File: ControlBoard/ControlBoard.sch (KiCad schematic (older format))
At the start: 76 parts, among them J1 PowerIn, J10 Conn_01x01, J11 Conn_01x01, J2 UART, J3 ICSP, J4 MTR1, J5 MTR2, J8 Conn_01x01, J9 Conn_01x01, Q1 2N3904, SW1 SW_Push, U1 LM358, U5 ATMEGA328P-PU, U6 LM7805_TO220, U7 74HC595, U8 L298D, U9 74HC595, Y1 16MHz

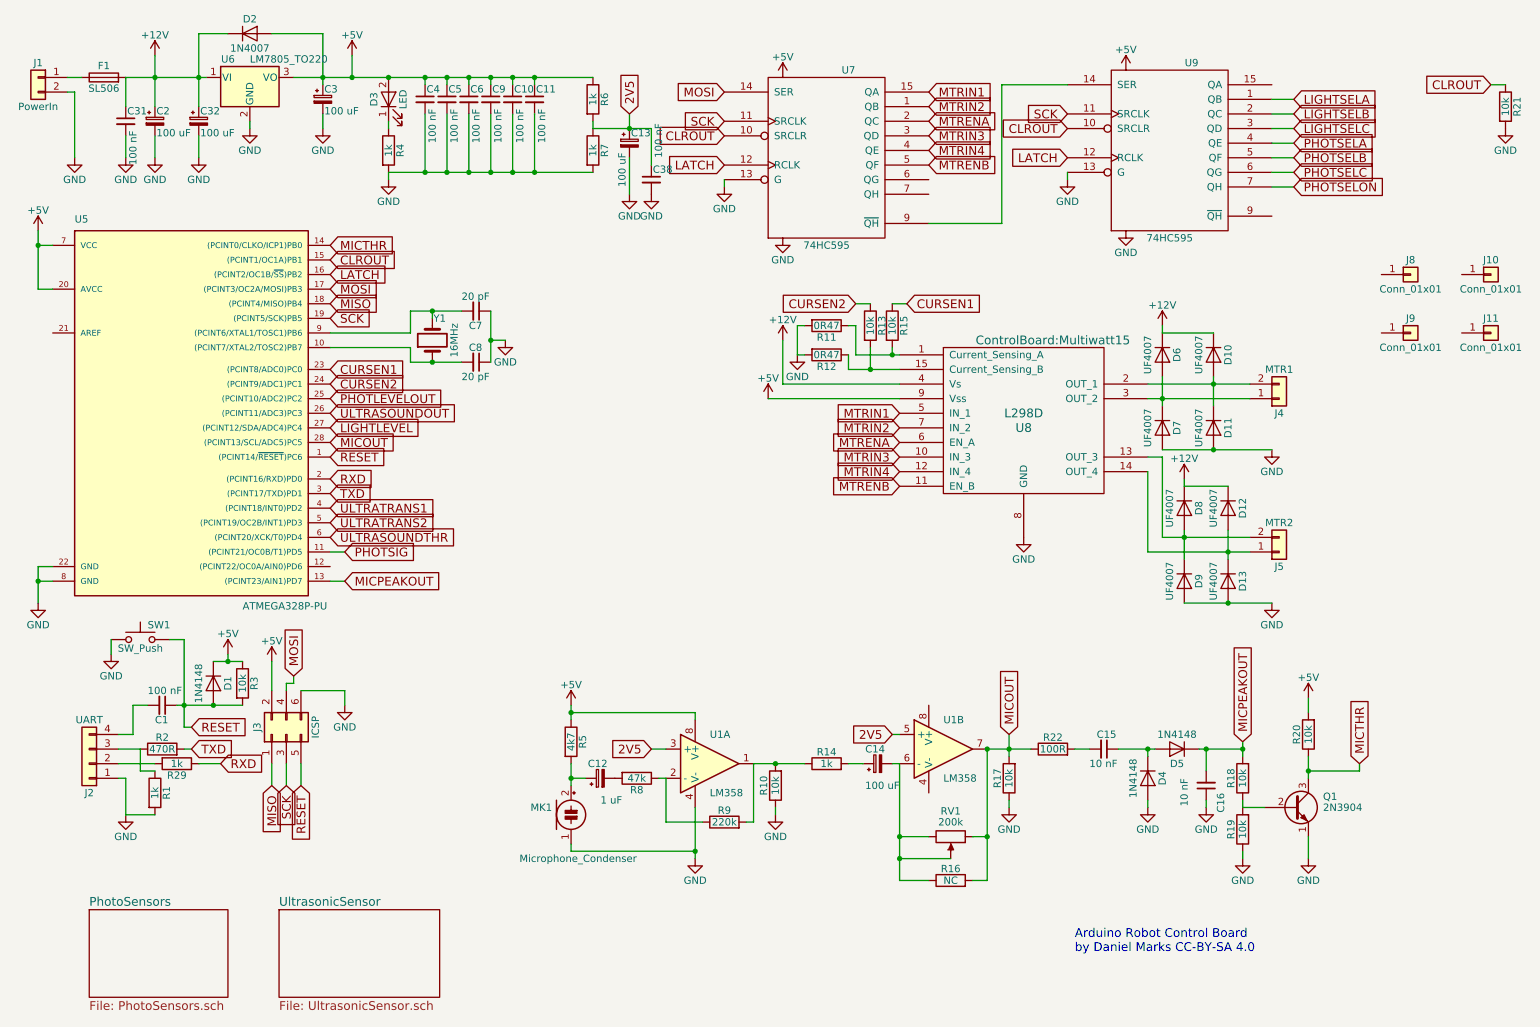
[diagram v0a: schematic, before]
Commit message: Added CAD models
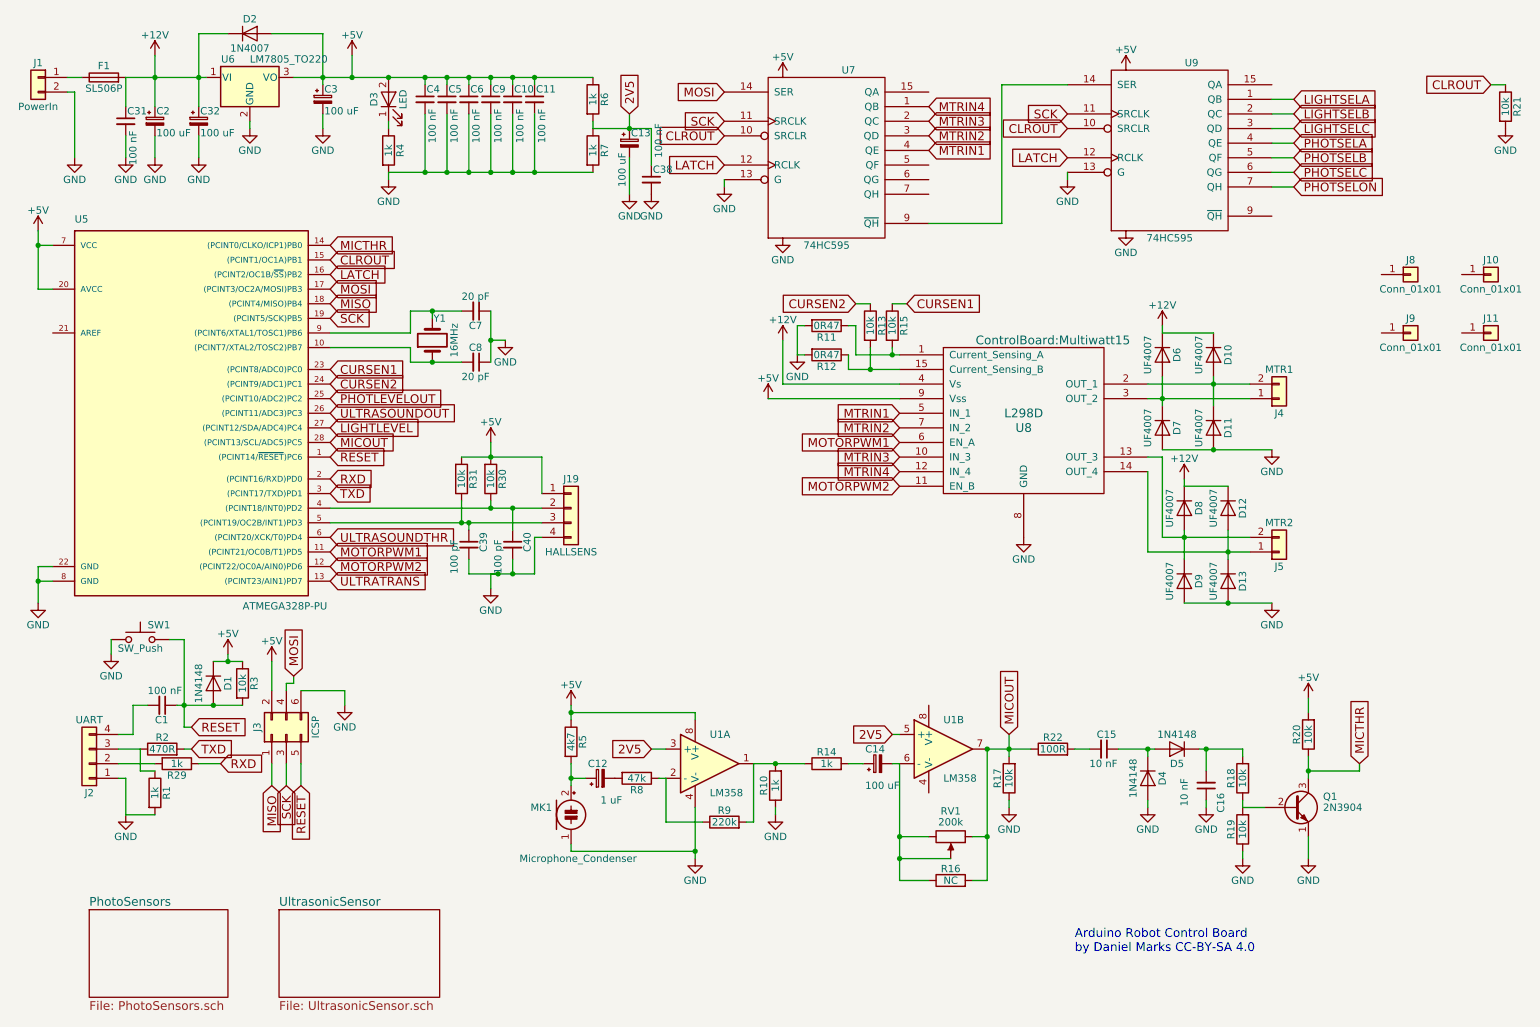
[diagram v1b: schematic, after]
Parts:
- added C39, C40: 100 pF, Capacitors_THT:C_Disc_D5.0mm_W2.5mm_P5.00mm, symbol C_Small
- added J19: HALLSENS, Pin_Headers:Pin_Header_Straight_1x04_Pitch2.54mm, symbol Conn_01x04
- added R30, R31: 10k, Resistors_THT:R_Axial_DIN0207_L6.3mm_D2.5mm_P7.62mm_Horizontal, symbol R
- F1: value SL506 -> SL506P
- R10: value 10k -> 1k
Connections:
- net PHOTSIG is gone; now on net MOTORPWM1: U5.11 ((PCINT21/OC0B/T1)PD5)
- net +5V: now also J19.1 (Pin_1), R30.2, R31.2
- net GND: now also C39.2, C40.2, J19.4 (Pin_4)
- net MTRIN1: now also U7.4 (QE); no longer U7.15 (QA)
- net MTRIN2: now also U7.3 (QD); no longer U7.1 (QB)
- net MTRIN3: now also U7.2 (QC); no longer U7.3 (QD)
- net MTRIN4: now also U7.1 (QB); no longer U7.4 (QE)
- net MOTORPWM2: now reaches U5.12 ((PCINT22/OC0A/AIN0)PD6)
- net MOTORPWM2: now also U8.11 (EN_B)
- net MICPEAKOUT: no longer names the net of C16.2, D5.1 (K), R18.2
- net MICPEAKOUT: no longer U5.13 ((PCINT23/AIN1)PD7)
- net MTRENA renamed MOTORPWM1
- net MOTORPWM1: no longer U7.2 (QC)
- net MTRENB: no longer names the net of U7.5 (QF)
- net MTRENB: no longer U8.11 (EN_B)
- net ULTRATRANS1: no longer names the net of U5.4 ((PCINT18/INT0)PD2)
- net ULTRATRANS1: now also C40.1, J19.2 (Pin_2), R30.1
- net ULTRATRANS2: no longer names the net of U5.5 ((PCINT19/OC2B/INT1)PD3)
- net ULTRATRANS2: now also C39.1, J19.3 (Pin_3), R31.1
- new net ULTRATRANS: U5.13 ((PCINT23/AIN1)PD7)

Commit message: Added KeypadPI
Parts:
- added C44, C45: 100 pF, Capacitors_THT:C_Disc_D5.0mm_W2.5mm_P5.00mm, symbol C_Small
- added C46: 100 nF, Capacitors_THT:C_Disc_D5.0mm_W2.5mm_P2.50mm, symbol C_Small
- added J20: Conn_01x06, Pin_Headers:Pin_Header_Straight_1x06_Pitch2.54mm, symbol Conn_01x06
- added J21: HALLSENS2, Pin_Headers:Pin_Header_Straight_1x04_Pitch2.54mm, symbol Conn_01x04
- added R34, R49, R65: 10k, Resistors_THT:R_Axial_DIN0207_L6.3mm_D2.5mm_P7.62mm_Horizontal, symbol R
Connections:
- net MISO is gone; now on net MICTHR: J3.1 (Pin_1), U5.18 ((PCINT4/MISO)PB4)
- net +5V: now also R21.1, J20.6 (Pin_6), J21.1 (Pin_1), R34.2, R49.2
- net CLROUT: now also R21.2, C46.1; no longer R21.1, U5.15 ((PCINT1/OC1A)PB1)
- net GND: now also C44.2, C45.2, C46.2, J20.1 (Pin_1), J21.4 (Pin_4); no longer R21.2
- net MICTHR: now also R65.2; no longer Q1.3 (C), R20.1, U5.14 ((PCINT0/CLKO/ICP1)PB0)
- net at U7.15 (QA): now also J20.5 (Pin_5)
- net at U7.5 (QF): now also J20.2 (Pin_2)
- net at U7.6 (QG): now also J20.3 (Pin_3)
- net at U7.7 (QH): now also J20.4 (Pin_4)
- new net: C45.1, J21.2 (Pin_2), R49.1, U5.14 ((PCINT0/CLKO/ICP1)PB0)
- new net: C44.1, J21.3 (Pin_3), R34.1, U5.15 ((PCINT1/OC1A)PB1)
- new net: Q1.3 (C), R20.1, R65.1
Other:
- moved on the sheet: C7, C8, R21, Y1

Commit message: JLCPCB order 2021-10-03
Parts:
- added C47: 100 uF, Capacitors_THT:CP_Radial_D5.0mm_P2.50mm, symbol CP_Small
- added J22: PowerIn, Connectors_Terminal_Blocks:TerminalBlock_bornier-2_P5.08mm, symbol Conn_01x02
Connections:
- net +5V: now also C47.1, J22.1 (Pin_1)
- net GND: now also C47.2, J22.2 (Pin_2)
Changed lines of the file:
@@
 $EndComp
 $Comp
-L GND #PWR50
+L GND #PWR53
 U 1 1 6146DC53
 P 10650 1800
-F 0 "#PWR50" H 10650 1550 50  0001 C CNN
+F 0 "#PWR53" H 10650 1550 50  0001 C CNN
 F 1 "GND" H 10650 1650 50  0000 C CNN
 F 2 "" H 10650 1800 50  0001 C CNN
@@
 Connection ~ 10650 1500
 $Comp
-L +5V #PWR49
+L +5V #PWR52
 U 1 1 614E555C
 P 10650 1000
-F 0 "#PWR49" H 10650 850 50  0001 C CNN
+F 0 "#PWR52" H 10650 850 50  0001 C CNN
 F 1 "+5V" H 10650 1140 50  0000 C CNN
 F 2 "" H 10650 1000 50  0001 C CNN
@@
 Wire Wire Line
 	9750 5150 9750 5250
+$Comp
+L Conn_01x02 J22
+U 1 1 6152297D
+P 9800 3250
+F 0 "J22" H 9800 3350 50  0000 C CNN
+F 1 "PowerIn" H 9800 3050 50  0000 C CNN
+F 2 "Connectors_Terminal_Blocks:TerminalBlock_bornier-2_P5.08mm" H 9800 3250 50  0001 C CNN
+F 3 "" H 9800 3250 50  0001 C CNN
+	1    9800 3250
+	-1   0    0    -1
+$EndComp
+$Comp
+L GND #PWR50
+U 1 1 61523138
+P 10100 3550
+F 0 "#PWR50" H 10100 3300 50  0001 C CNN
+F 1 "GND" H 10100 3400 50  0000 C CNN
+F 2 "" H 10100 3550 50  0001 C CNN
+F 3 "" H 10100 3550 50  0001 C CNN
+	1    10100 3550
+	1    0    0    -1
+$EndComp
+Wire Wire Line
+	10100 3550 10100 3350
+Wire Wire Line
+	10100 3350 10000 3350
+$Comp
+L +5V #PWR49
+U 1 1 61523719
+P 10100 3050
+F 0 "#PWR49" H 10100 2900 50  0001 C CNN
+F 1 "+5V" H 10100 3190 50  0000 C CNN
+F 2 "" H 10100 3050 50  0001 C CNN
+F 3 "" H 10100 3050 50  0001 C CNN
+	1    10100 3050
+	1    0    0    -1
+$EndComp
+Wire Wire Line
+	10100 3050 10100 3250
+Wire Wire Line
+	10000 3250 10400 3250
+$Comp
+L CP_Small C47
+U 1 1 61523E68
+P 10400 3350
+F 0 "C47" H 10410 3420 50  0000 L CNN
+F 1 "100 uF" H 10410 3270 50  0000 L CNN
+F 2 "Capacitors_THT:CP_Radial_D5.0mm_P2.50mm" H 10400 3350 50  0001 C CNN
+F 3 "" H 10400 3350 50  0001 C CNN
+	1    10400 3350
+	1    0    0    -1
+$EndComp
+Connection ~ 10100 3250
+$Comp
+L GND #PWR51
+U 1 1 61524424
+P 10400 3550
+F 0 "#PWR51" H 10400 3300 50  0001 C CNN
+F 1 "GND" H 10400 3400 50  0000 C CNN
+F 2 "" H 10400 3550 50  0001 C CNN
+F 3 "" H 10400 3550 50  0001 C CNN
+	1    10400 3550
+	1    0    0    -1
+$EndComp
+Wire Wire Line
+	10400 3450 10400 3550
 $EndSCHEMATC

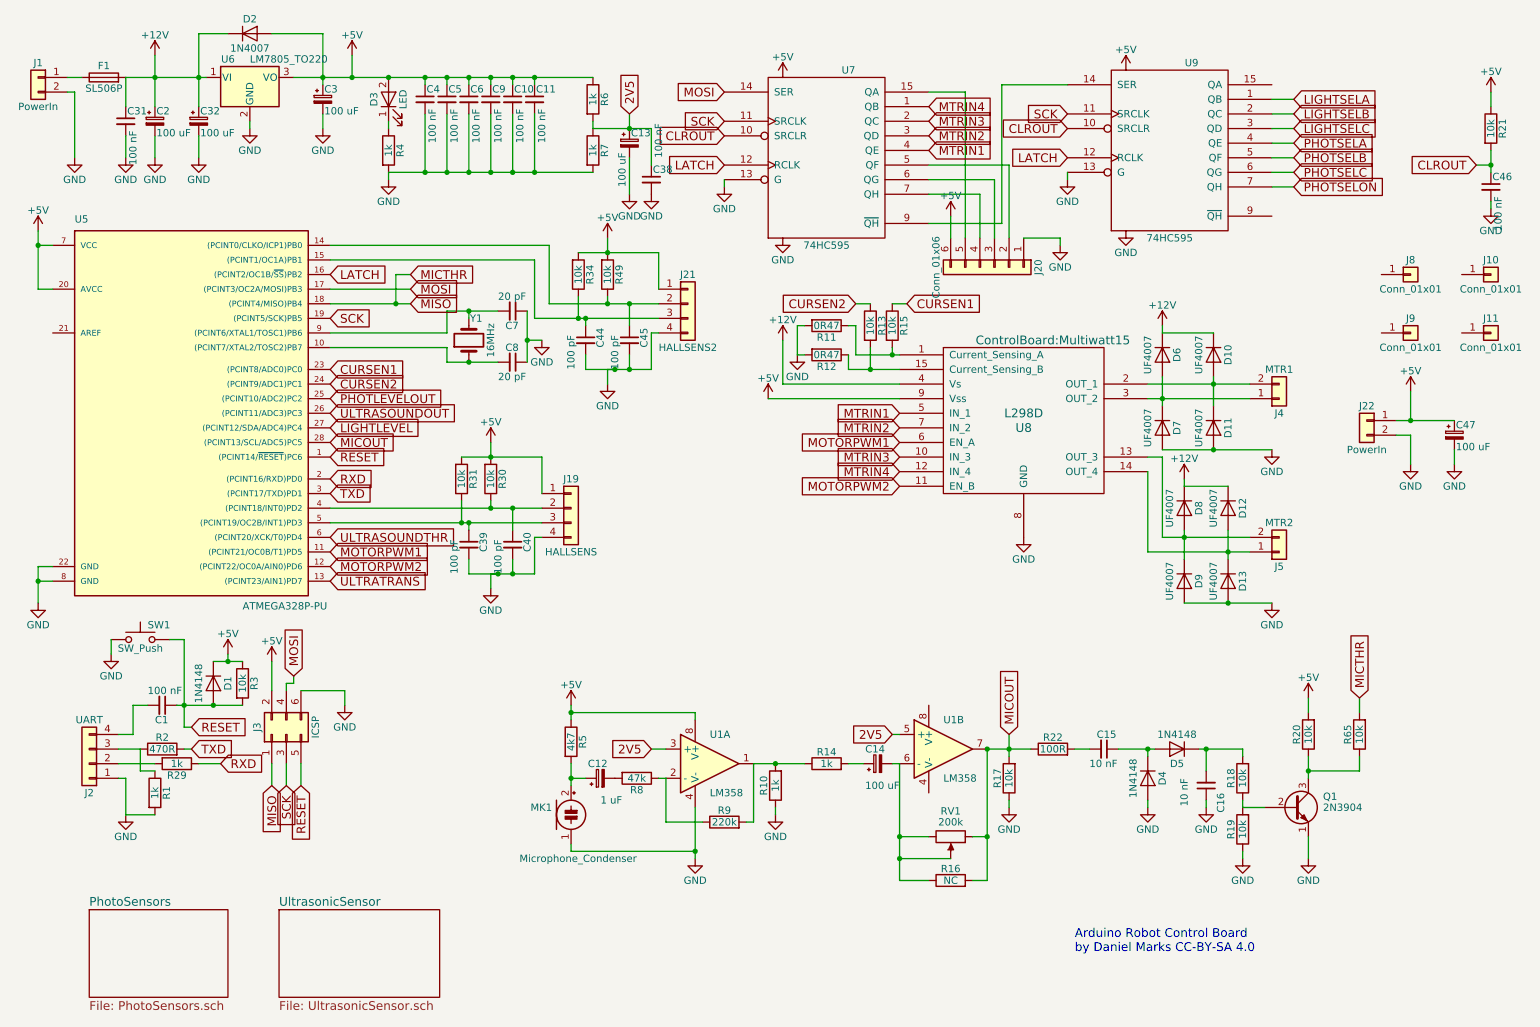
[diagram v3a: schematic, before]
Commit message: Begin code for controlling robot with command line
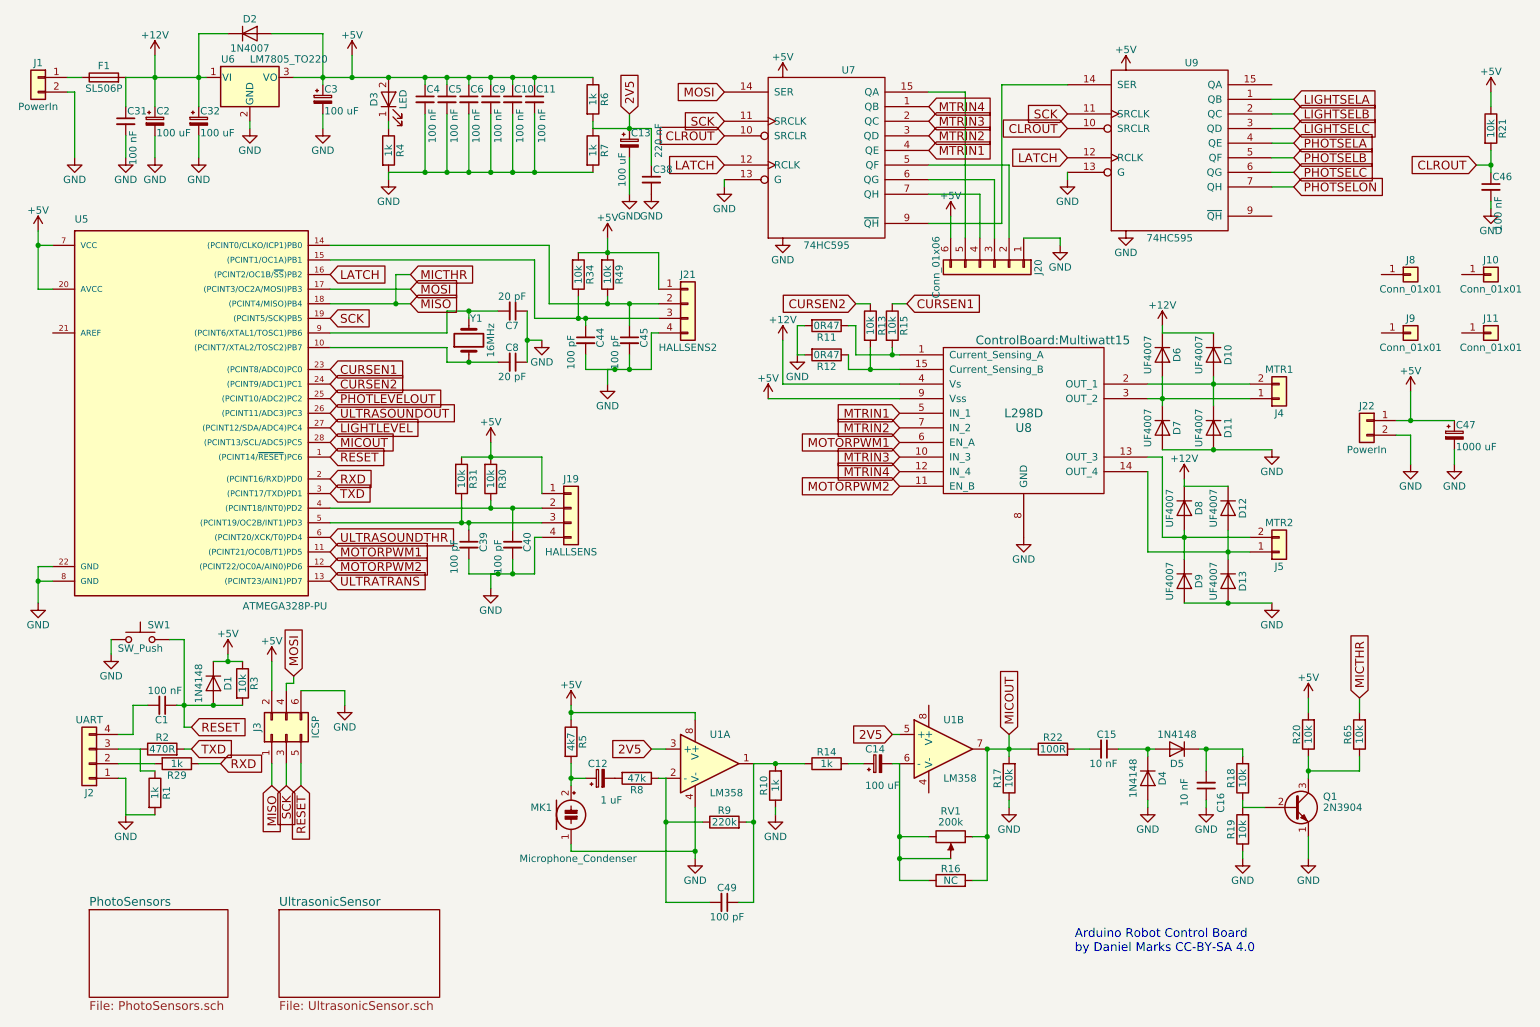
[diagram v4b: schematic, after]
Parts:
- added C49: 100 pF, Capacitors_THT:C_Disc_D5.0mm_W2.5mm_P5.00mm, symbol C_Small
- C38: value 100 nF -> 220 nF
- C47: value 100 uF -> 1000 uF; footprint Capacitors_THT:CP_Radial_D5.0mm_P2.50mm -> Capacitors_THT:CP_Radial_D7.5mm_P2.50mm
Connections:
- net at R10.2, R14.1, R9.2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: now also C49.1
- net at R8.1, R9.1, U1.2 (-): now also C49.2
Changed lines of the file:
@@
 P 4900 1600
 F 0 "C38" H 4910 1670 50  0000 L CNN
-F 1 "100 nF" V 4950 1750 50  0000 L CNN
+F 1 "220 nF" V 4950 1750 50  0000 L CNN
 F 2 "Capacitors_THT:C_Disc_D5.0mm_W2.5mm_P2.50mm" H 4900 1600 50  0001 C CNN
 F 3 "" H 4900 1600 50  0001 C CNN
@@
 	5600 5600 5950 5600
 Wire Wire Line
-	5000 6000 5000 5700
+	5000 5700 5000 6550
 Wire Wire Line
 	5250 6000 5000 6000
@@
 	5600 6000 5550 6000
 Wire Wire Line
-	5600 5600 5600 6000
+	5600 5600 5600 6550
 Wire Wire Line
 	5000 5500 4900 5500
@@
 P 10400 3350
 F 0 "C47" H 10410 3420 50  0000 L CNN
-F 1 "100 uF" H 10410 3270 50  0000 L CNN
-F 2 "Capacitors_THT:CP_Radial_D5.0mm_P2.50mm" H 10400 3350 50  0001 C CNN
+F 1 "1000 uF" H 10410 3270 50  0000 L CNN
+F 2 "Capacitors_THT:CP_Radial_D7.5mm_P2.50mm" H 10400 3350 50  0001 C CNN
 F 3 "" H 10400 3350 50  0001 C CNN
 	1    10400 3350
@@
 Wire Wire Line
 	10400 3450 10400 3550
+$Comp
+L C_Small C49
+U 1 1 6197F638
+P 5400 6550
+F 0 "C49" V 5300 6500 50  0000 L CNN
+F 1 "100 pF" V 5500 6450 50  0000 L CNN
+F 2 "Capacitors_THT:C_Disc_D5.0mm_W2.5mm_P5.00mm" H 5400 6550 50  0001 C CNN
+F 3 "" H 5400 6550 50  0001 C CNN
+	1    5400 6550
+	0    1    1    0
+$EndComp
+Wire Wire Line
+	5600 6550 5500 6550
+Connection ~ 5600 6000
+Wire Wire Line
+	5000 6550 5300 6550
+Connection ~ 5000 6000
 $EndSCHEMATC
